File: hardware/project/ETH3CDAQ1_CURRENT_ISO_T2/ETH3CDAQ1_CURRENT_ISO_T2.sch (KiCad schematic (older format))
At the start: 83 parts, among them J1 GMSTB2,5/2-GF-7,62, J2 Conn_02x10_Odd_Even, K1 G5Q-1, U1 DG211, U10 74LVC1GU04DRL, U11 74LVC1GU04DRL, U12 74LVC1GU04DRL, U13 24LC08B-E/MS, U14 TXB0104PW, U15 PCA9557PW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

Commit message: PCB layout
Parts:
- D1: footprint (none) -> Diode_SMD:D_SOD-123
- R1, R2: footprint (none) -> Resistor_SMD:R_0603_1608Metric_Pad0.98x0.95mm_HandSolder
- U16: footprint (none) -> Package_SO:SOIC-8_3.9x4.9mm_P1.27mm
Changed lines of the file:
@@
 F 0 "U16" H 4250 3100 50  0000 L CNN
 F 1 "OPA132" H 4150 3000 50  0000 L CNN
-F 2 "" H 4100 2900 50  0001 C CNN
+F 2 "Package_SO:SOIC-8_3.9x4.9mm_P1.27mm" H 4100 2900 50  0001 C CNN
 F 3 "" H 4100 3000 50  0001 C CNN
 	1    4050 2850
@@
 F 0 "R1" V 3193 2950 50  0000 C CNN
 F 1 "100k" V 3284 2950 50  0000 C CNN
-F 2 "" V 3330 2950 50  0001 C CNN
+F 2 "Resistor_SMD:R_0603_1608Metric_Pad0.98x0.95mm_HandSolder" V 3330 2950 50  0001 C CNN
 F 3 "~" H 3400 2950 50  0001 C CNN
 	1    3400 2950
@@
 F 0 "R2" V 3193 3500 50  0000 C CNN
 F 1 "316" V 3284 3500 50  0000 C CNN
-F 2 "" V 3330 3500 50  0001 C CNN
+F 2 "Resistor_SMD:R_0603_1608Metric_Pad0.98x0.95mm_HandSolder" V 3330 3500 50  0001 C CNN
 F 3 "~" H 3400 3500 50  0001 C CNN
 	1    3400 3500
@@
 Y16285R00000D0W
 $Comp
-L Diode:1N4148W D1
-U 1 1 609F2E3E
-P 4150 800
-F 0 "D1" H 4150 1017 50  0000 C CNN
-F 1 "1N4148W" H 4150 926 50  0000 C CNN
-F 2 "" H 4150 625 50  0001 C CNN
-F 3 "https://www.vishay.com/docs/85748/1n4148w.pdf" H 4150 800 50  0001 C CNN
-	1    4150 800
-	1    0    0    -1
-$EndComp
-$Comp
 L power:GND #PWR0112
 U 1 1 609F9DC9
@@
 	3750 800  3800 800
 Connection ~ 3800 800
+$Comp
+L Diode:1N4148W D1
+U 1 1 5FC7CD0F
+P 4150 800
+F 0 "D1" H 4150 1017 50  0000 C CNN
+F 1 "1N4148W" H 4150 926 50  0000 C CNN
+F 2 "Diode_SMD:D_SOD-123" H 4150 625 50  0001 C CNN
+F 3 "https://www.vishay.com/docs/85748/1n4148w.pdf" H 4150 800 50  0001 C CNN
+	1    4150 800
+	1    0    0    -1
+$EndComp
 $EndSCHEMATC

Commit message: PCB design
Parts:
- added C32: 10u, Capacitor_SMD:C_0603_1608Metric_Pad1.08x0.95mm_HandSolder, symbol Device:C
- added C33: 100n, Capacitor_SMD:C_0603_1608Metric_Pad1.08x0.95mm_HandSolder, symbol Device:C
- C14, C15: value 100n -> 10u
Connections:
- net +5V: now also C32.1, C33.1
- net GND: now also C32.2, C33.2
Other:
- moved on the sheet: C26, C27, C28, C29, FB2, FB3

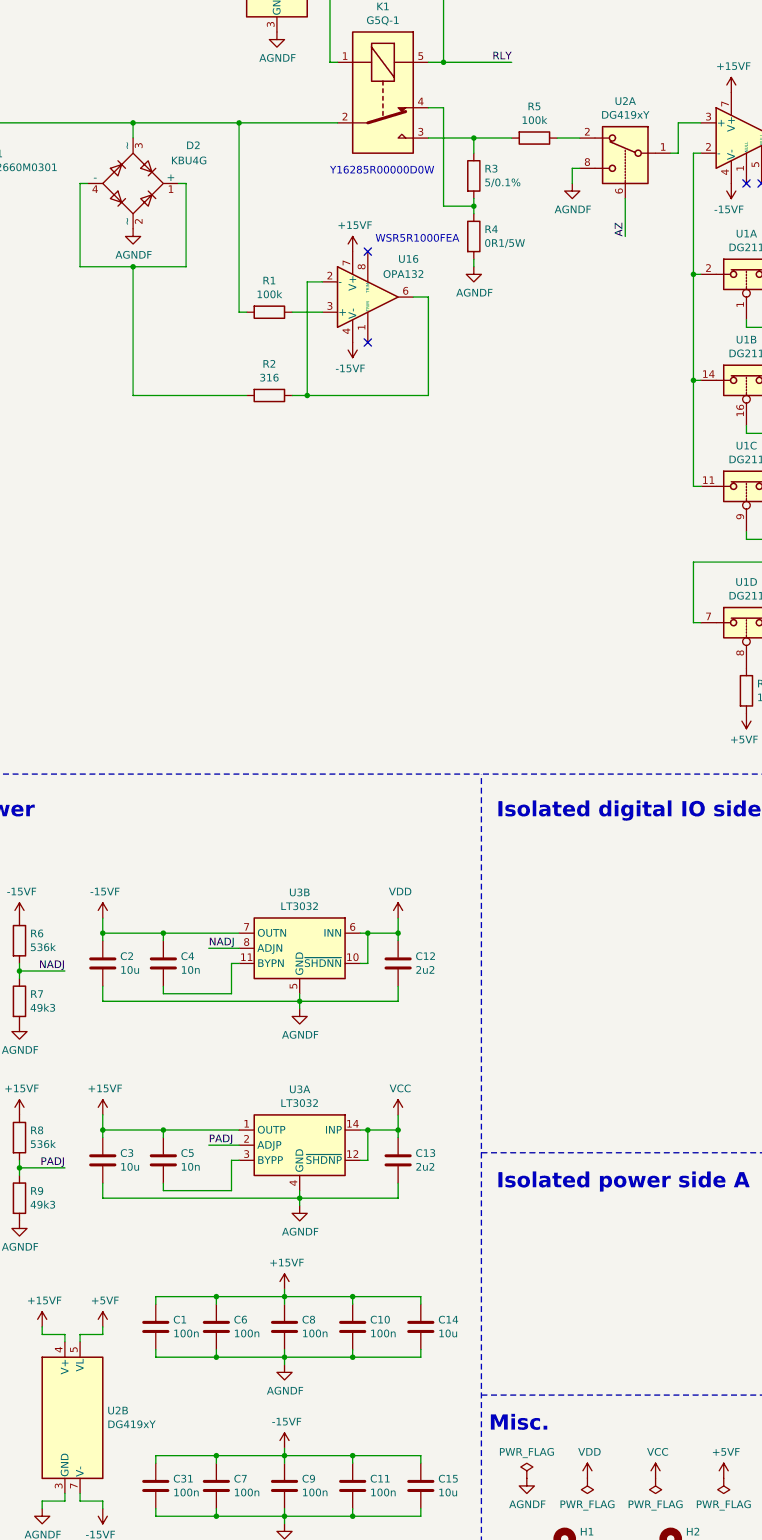
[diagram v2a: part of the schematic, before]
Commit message: Fixed mistake with DG419. Never use DG419Lxx variant.
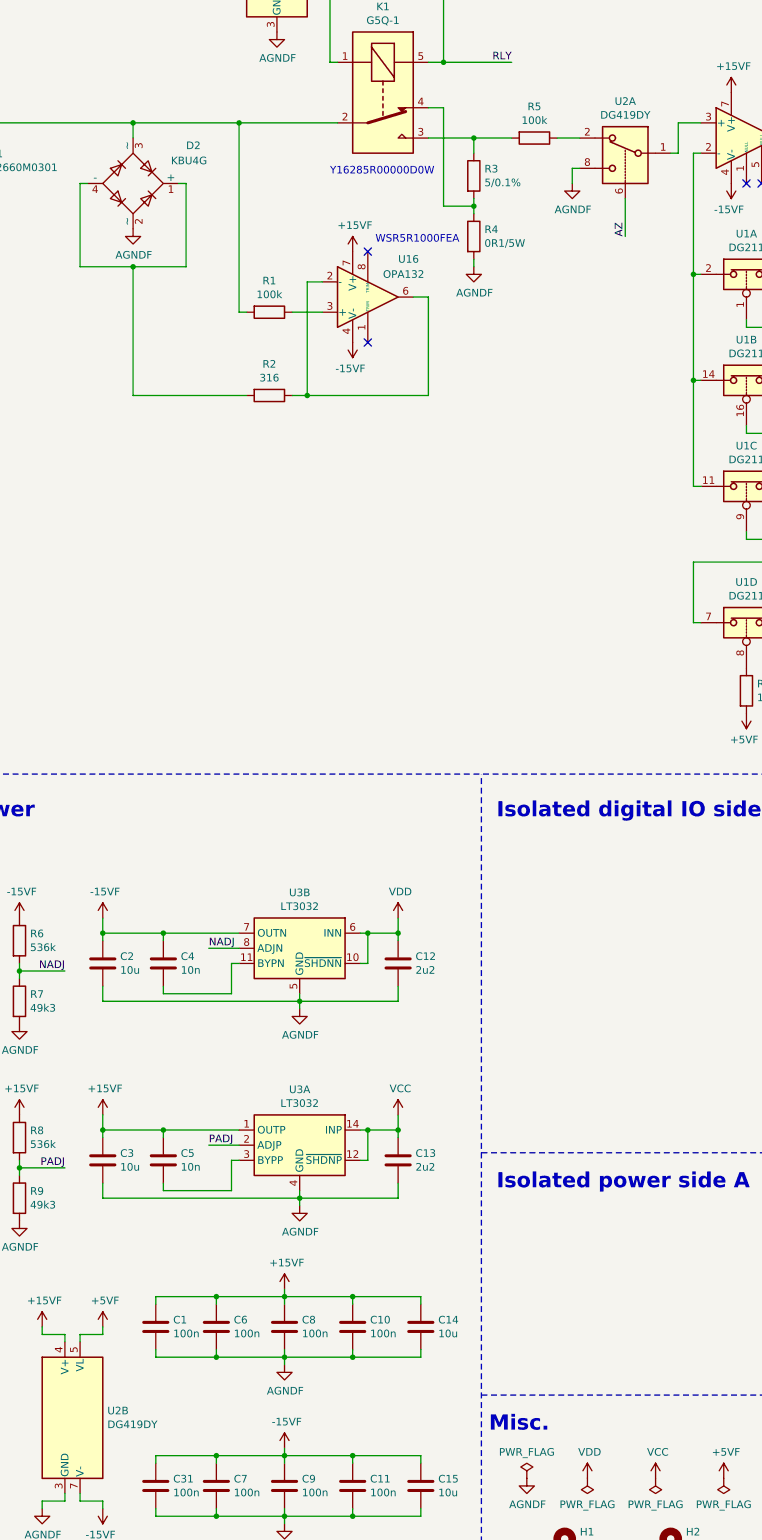
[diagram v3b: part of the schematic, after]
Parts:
- U2: value DG419xY -> DG419DY
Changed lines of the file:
@@
 P 5750 1800
 F 0 "U2" H 5750 2042 50  0000 C CNN
-F 1 "DG419xY" H 5750 1951 50  0000 C CNN
+F 1 "DG419DY" H 5750 1951 50  0000 C CNN
 F 2 "Package_SO:SOIC-8_3.9x4.9mm_P1.27mm" H 5750 1500 50  0001 C CNN
 F 3 "https://datasheets.maximintegrated.com/en/ds/DG417-DG419.pdf" H 5750 1800 50  0001 C CNN
@@
 P 2050 10250
 F 0 "U2" H 2330 10296 50  0000 L CNN
-F 1 "DG419xY" H 2330 10205 50  0000 L CNN
+F 1 "DG419DY" H 2330 10205 50  0000 L CNN
 F 2 "Package_SO:SOIC-8_3.9x4.9mm_P1.27mm" H 2050 9950 50  0001 C CNN
 F 3 "https://datasheets.maximintegrated.com/en/ds/DG417-DG419.pdf" H 2050 10250 50  0001 C CNN
